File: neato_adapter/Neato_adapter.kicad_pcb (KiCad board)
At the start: 2 copper layers, 43 x 21 mm, 9 parts, among them J1 JST PH B4B Vert, J2 JST PH B2B Vert, J3 JST PH B4B Vert, Q1 AS2302, U1 DNP LM2596

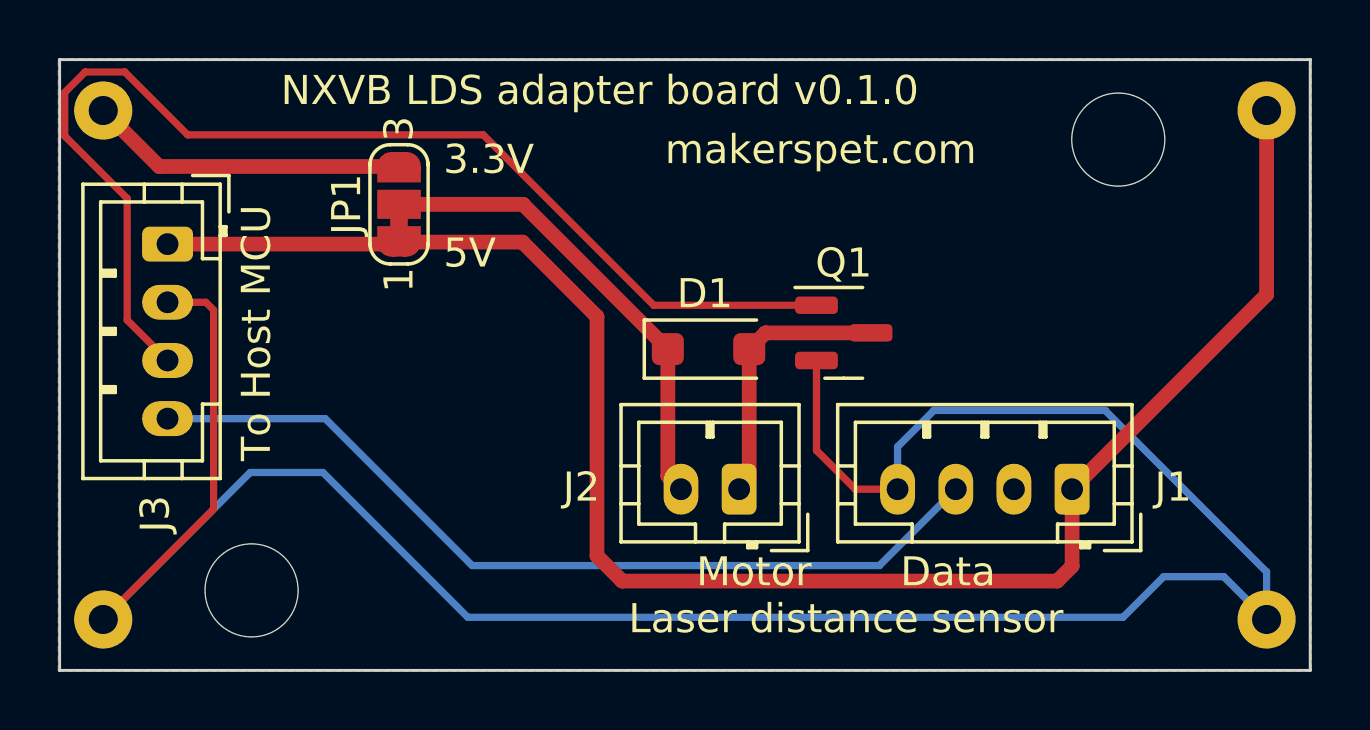
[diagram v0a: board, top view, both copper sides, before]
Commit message: Neato, LDS02RR v0.2.0
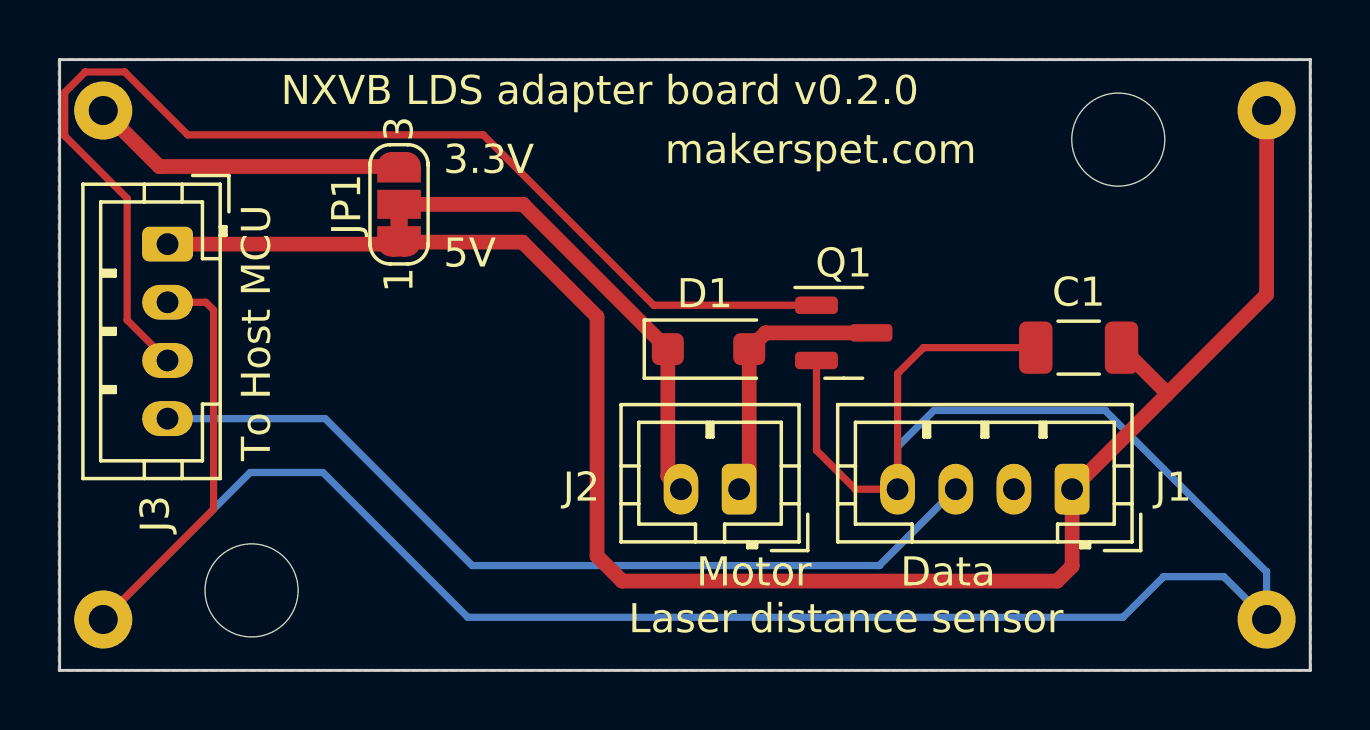
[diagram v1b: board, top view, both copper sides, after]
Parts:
- added C1: 100uF, Capacitor_SMD:C_1206_3216Metric, F.Cu at (113.5, 49.4)
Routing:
- net GND: track 84.3 -> 93.4 mm
- net +5V: track 59.4 -> 61.7 mm
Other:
- board text added: "NXVB LDS adapter board v0.2.0"
- board text removed: "NXVB LDS adapter board v0.1.0"
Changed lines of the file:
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@@
     (fp_line (start 7.95 2.8) (end 7.95 -1.7)
       (stroke (width 0.1) (type solid)) (layer "F.Fab"))
-    (pad "1" thru_hole roundrect (at 0 0 270) (size 1.2 1.75) (drill 0.75) (layers "*.Cu" "*.Mask") (roundrect_rratio 0.2083333333)
+    (pad "1" thru_hole roundrect (at 0 0 270) (size 1.2 1.75) (drill 0.75) (layers "*.Cu" "*.Mask") (roundrect_rratio 0.208333)
       (net 1 "+5V") (pinfunction "Pin_1") (pintype "passive"))
     (pad "2" thru_hole oval (at 2 0 270) (size 1.2 1.75) (drill 0.75) (layers "*.Cu" "*.Mask")
@@
     (fp_line (start 3.95 2.8) (end 3.95 -1.7)
       (stroke (width 0.1) (type solid)) (layer "F.Fab"))
-    (pad "1" thru_hole roundrect (at 0 0 180) (size 1.2 1.75) (drill 0.75) (layers "*.Cu" "*.Mask") (roundrect_rratio 0.2083333333)
+    (pad "1" thru_hole roundrect (at 0 0 180) (size 1.2 1.75) (drill 0.75) (layers "*.Cu" "*.Mask") (roundrect_rratio 0.208333)
       (net 2 "/MOT-") (pinfunction "Pin_1") (pintype "passive"))
     (pad "2" thru_hole oval (at 2 0 180) (size 1.2 1.75) (drill 0.75) (layers "*.Cu" "*.Mask")
@@
         (effects (font (size 1 1) (thickness 0.15)))
     )
+    (fp_text user "3" (at 2.6 0 90) (layer "F.SilkS")
+        (effects (font (size 1 1) (thickness 0.15)))
+    )
     (fp_text user "1" (at -2.6 0 90) (layer "F.SilkS")
-        (effects (font (size 1 1) (thickness 0.15)))
-    )
-    (fp_text user "3" (at 2.6 0 90) (layer "F.SilkS")
         (effects (font (size 1 1) (thickness 0.15)))
     )
@@
     (fp_line (start 7.95 2.8) (end 7.95 -1.7)
       (stroke (width 0.1) (type solid)) (layer "F.Fab"))
-    (pad "1" thru_hole roundrect (at 0 0 180) (size 1.2 1.75) (drill 0.75) (layers "*.Cu" "*.Mask") (roundrect_rratio 0.2083333333)
+    (pad "1" thru_hole roundrect (at 0 0 180) (size 1.2 1.75) (drill 0.75) (layers "*.Cu" "*.Mask") (roundrect_rratio 0.208333)
       (net 1 "+5V") (pinfunction "Pin_1") (pintype "passive"))
     (pad "2" thru_hole oval (at 2 0 180) (size 1.2 1.75) (drill 0.75) (layers "*.Cu" "*.Mask")
@@
     )
   )
+  (footprint "Capacitor_SMD:C_1206_3216Metric" (layer "F.Cu")
+    (at 113.538 49.403 180)
+    (descr "Capacitor SMD 1206 (3216 Metric), square (rectangular) end terminal, IPC_7351 nominal, (Body size source: IPC-SM-782 page 76, https://www.pcb-3d.com/wordpress/wp-content/uploads/ipc-sm-782a_amendment_1_and_2.pdf), generated with kicad-footprint-generator")
+    (tags "capacitor")
+    (property "Sheetfile" "Neato_adapter.kicad_sch")
+    (property "Sheetname" "")
+    (property "ki_description" "Unpolarized capacitor")
+    (property "ki_keywords" "cap capacitor")
+    (attr smd)
+    (fp_text reference "C1" (at 0 1.905) (layer "F.SilkS")
+        (effects (font (size 1 1) (thickness 0.15)))
+    )
+    (fp_text value "100uF" (at 0 1.85) (layer "F.Fab") hide
+        (effects (font (size 1 1) (thickness 0.15)))
+    )
+    (fp_text user "${REFERENCE}" (at 0 0) (layer "F.Fab")
+        (effects (font (size 0.8 0.8) (thickness 0.12)))
+    )
+    (fp_line (start -0.711252 -0.91) (end 0.711252 -0.91)
+      (stroke (width 0.12) (type solid)) (layer "F.SilkS"))
+    (fp_line (start -0.711252 0.91) (end 0.711252 0.91)
+      (stroke (width 0.12) (type solid)) (layer "F.SilkS"))
+    (fp_line (start -2.3 -1.15) (end 2.3 -1.15)
+      (stroke (width 0.05) (type solid)) (layer "F.CrtYd"))
+    (fp_line (start -2.3 1.15) (end -2.3 -1.15)
+      (stroke (width 0.05) (type solid)) (layer "F.CrtYd"))
+    (fp_line (start 2.3 -1.15) (end 2.3 1.15)
+      (stroke (width 0.05) (type solid)) (layer "F.CrtYd"))
+    (fp_line (start 2.3 1.15) (end -2.3 1.15)
+      (stroke (width 0.05) (type solid)) (layer "F.CrtYd"))
+    (fp_line (start -1.6 -0.8) (end 1.6 -0.8)
+      (stroke (width 0.1) (type solid)) (layer "F.Fab"))
+    (fp_line (start -1.6 0.8) (end -1.6 -0.8)
+      (stroke (width 0.1) (type solid)) (layer "F.Fab"))
+    (fp_line (start 1.6 -0.8) (end 1.6 0.8)
+      (stroke (width 0.1) (type solid)) (layer "F.Fab"))
+    (fp_line (start 1.6 0.8) (end -1.6 0.8)
+      (stroke (width 0.1) (type solid)) (layer "F.Fab"))
+    (pad "1" smd roundrect (at -1.475 0 180) (size 1.15 1.8) (layers "F.Cu" "F.Paste" "F.Mask") (roundrect_rratio 0.217391)
+      (net 1 "+5V") (pintype "passive"))
+    (pad "2" smd roundrect (at 1.475 0 180) (size 1.15 1.8) (layers "F.Cu" "F.Paste" "F.Mask") (roundrect_rratio 0.217391)
+      (net 5 "GND") (pintype "passive"))
+    (model "${KICAD6_3DMODEL_DIR}/Capacitor_SMD.3dshapes/C_1206_3216Metric.wrl"
+      (offset (xyz 0 0 0))
+      (scale (xyz 1 1 1))
+      (rotate (xyz 0 0 0))
+    )
+  )
   (footprint "MountingHole:MountingHole_3.2mm_M3" (layer "F.Cu")
     (at 85.1 57.75)
@@
   (footprint "Makerspet:LM2596 Module" (layer "B.Cu")
     (at 100 50 180)
+    (descr "DC-DC voltage regulator module")
     (property "Link" "")
     (property "Sheetfile" "Neato_adapter.kicad_sch")
@@
         (effects (font (size 1 1) (thickness 0.15)) (justify mirror))
     )
+    (fp_text user "IN+" (at -20.65 5.296 unlocked) (layer "B.SilkS")
+        (effects (font (size 1 1) (thickness 0.1)) (justify left bottom mirror))
+    )
+    (fp_text user "IN-" (at -20.65 -6.642 unlocked) (layer "B.SilkS")
+        (effects (font (size 1 1) (thickness 0.1)) (justify left bottom mirror))
+    )
     (fp_text user "OUT+" (at 17.196 5.296 unlocked) (layer "B.SilkS")
         (effects (font (size 1 1) (thickness 0.1)) (justify left bottom mirror))
     )
-    (fp_text user "IN+" (at -20.65 5.296 unlocked) (layer "B.SilkS")
-        (effects (font (size 1 1) (thickness 0.1)) (justify left bottom mirror))
-    )
     (fp_text user "OUT-" (at 17.196 -6.642 unlocked) (layer "B.SilkS")
-        (effects (font (size 1 1) (thickness 0.1)) (justify left bottom mirror))
-    )
-    (fp_text user "IN-" (at -20.65 -6.642 unlocked) (layer "B.SilkS")
         (effects (font (size 1 1) (thickness 0.1)) (justify left bottom mirror))
     )
@@
     (pad "4" thru_hole circle (at -20 8.75 180) (size 2 2) (drill 1) (layers "*.Cu" "*.Mask")
       (net 1 "+5V") (pinfunction "VIN+") (pintype "power_in"))
-    (model "C:/Users/ilya/git/snoopy/kicad/step/LM2596 DC-DC StepDown Converter v1.step"
+    (model "C:/Users/ilya/git/pcb/step/LM2596 DC-DC StepDown Converter v1.step"
       (offset (xyz 21.5 -0.5 12.5))
       (scale (xyz 1 1 1))
@@
     (effects (font (size 1 1) (thickness 0.15)) (justify bottom))
   )
-  (gr_text "NXVB LDS adapter board v0.1.0" (at 86.106 41.148) (layer "F.SilkS")
+  (gr_text "NXVB LDS adapter board v0.2.0" (at 86.106 41.148) (layer "F.SilkS")
     (effects (font (size 1 1) (thickness 0.15)) (justify left bottom))
   )
@@
   (segment (start 112.8014 57.4294) (end 97.8408 57.4294) (width 0.508) (layer "F.Cu") (net 1))
   (segment (start 94.4164 45.7754) (end 90.17 45.7754) (width 0.508) (layer "F.Cu") (net 1))
-  (segment (start 120 47.5832) (end 113.3122 54.271) (width 0.508) (layer "F.Cu") (net 1))
+  (segment (start 115.013 49.403) (end 116.5576 50.9476) (width 0.508) (layer "F.Cu") (net 1))
+  (segment (start 116.5576 50.9476) (end 116.5576 51.0256) (width 0.508) (layer "F.Cu") (net 1))
   (segment (start 96.9772 48.3362) (end 94.4164 45.7754) (width 0.508) (layer "F.Cu") (net 1))
   (segment (start 96.9772 56.5658) (end 96.9772 48.3362) (width 0.508) (layer "F.Cu") (net 1))
+  (segment (start 116.5576 51.0256) (end 113.3122 54.271) (width 0.508) (layer "F.Cu") (net 1))
   (segment (start 120 41.25) (end 120 47.5832) (width 0.508) (layer "F.Cu") (net 1))
   (segment (start 90.1012 45.8442) (end 90.17 45.7754) (width 0.508) (layer "F.Cu") (net 1))
@@
   (segment (start 97.8408 57.4294) (end 96.9772 56.5658) (width 0.508) (layer "F.Cu") (net 1))
   (segment (start 82.211 45.8442) (end 90.1012 45.8442) (width 0.508) (layer "F.Cu") (net 1))
+  (segment (start 120 47.5832) (end 116.5576 51.0256) (width 0.508) (layer "F.Cu") (net 1))
   (segment (start 102.2126 49.4538) (end 102.2126 53.9218) (width 0.508) (layer "F.Cu") (net 2))
   (segment (start 106.3983 48.895) (end 102.7714 48.895) (width 0.508) (layer "F.Cu") (net 2))
@@
   (segment (start 92.6846 56.896) (end 87.6328 51.8442) (width 0.25) (layer "B.Cu") (net 4))
   (segment (start 83.5312 47.8442) (end 82.211 47.8442) (width 0.25) (layer "F.Cu") (net 5))
+  (segment (start 112.063 49.403) (end 108.204 49.403) (width 0.25) (layer "F.Cu") (net 5))
   (segment (start 105.8584 54.271) (end 107.3122 54.271) (width 0.25) (layer "F.Cu") (net 5))
   (segment (start 83.7946 48.1076) (end 83.5312 47.8442) (width 0.25) (layer "F.Cu") (net 5))
   (segment (start 104.5233 49.845) (end 104.5233 52.9359) (width 0.25) (layer "F.Cu") (net 5))
   (segment (start 80 58.75) (end 83.7946 54.9554) (width 0.25) (layer "F.Cu") (net 5))
+  (segment (start 107.3122 50.2948) (end 107.3122 54.271) (width 0.25) (layer "F.Cu") (net 5))
   (segment (start 83.7946 54.9554) (end 83.7946 48.1076) (width 0.25) (layer "F.Cu") (net 5))
   (segment (start 104.5233 52.9359) (end 105.8584 54.271) (width 0.25) (layer "F.Cu") (net 5))
+  (segment (start 108.204 49.403) (end 107.3122 50.2948) (width 0.25) (layer "F.Cu") (net 5))
   (segment (start 120 58.75) (end 120 57.1096) (width 0.25) (layer "B.Cu") (net 5))
   (segment (start 92.5322 58.674) (end 87.5538 53.6956) (width 0.25) (layer "B.Cu") (net 5))
